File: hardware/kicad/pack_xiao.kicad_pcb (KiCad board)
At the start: 2 copper layers, 96 x 112 mm, 120 parts, among them U1 MCP1640T-I/CHY

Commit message: hardware: pack_xiao iron-only (plated holes under XIAO pads 16/20) and fits the enclosure (notch + cutout for the carrier posts)
Footprint XIAO_ESP32S3_SMD_THB (derived by tools/import_xiao.py) makes the two used bottom pads
plated holes, soldered from the board's back. gen_pcb learns NOTCH_BL and CUTOUTS (with a
no-copper fence, the router ignores edge clearance on inner circles); pack_xiao check_posts()
holds them to mech/params. make mech also gates --boards pack_xiao,carrier.

Co-Authored-By: Claude Opus 5.5 <noreply@anthropic.com>
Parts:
- removed the U_MCU at (78.0, 90.8)
- added U_MCU: XIAO ESP32-S3, local:XIAO_ESP32S3_SMD_THB, F.Cu at (76.0, 90.8)
- moved C_MCU1 2.00 mm to (55.5, 103.9)
- moved C_MCU2 2.00 mm to (55.5, 99.5)
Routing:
- net +3V3: track 170.5 -> 199.2 mm, vias 7 -> 6
- net VPACK: track 135.7 -> 111.4 mm, vias 2 -> 0
- net NTC3: track 84.0 -> 61.2 mm, vias 3 -> 2
- net SW1_DRV: track 120.3 -> 103.6 mm, vias 4 -> 2
- net CELL1_S: track 34.6 -> 18.2 mm, vias 0 -> 2
- net NTC2: track 102.6 -> 87.0 mm, vias 2 -> 0
- net CHG_CE: track 39.2 -> 54.4 mm
- net +5V: track 104.6 -> 91.6 mm
- net VMCU_IN: track 136.0 -> 147.3 mm
- net CC2: track 16.6 -> 26.9 mm, vias 0 -> 1
- net SYS_CHG: track 68.3 -> 58.0 mm, vias 4 -> 3
- net SW1_G: track 45.8 -> 55.7 mm
- net CELL4_G: track 22.1 -> 31.7 mm, vias 3 -> 2
- net SW3_DRV: track 66.9 -> 57.6 mm
- net SYS: track 107.8 -> 98.5 mm, vias 2 -> 0
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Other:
- outline, holes or cut-outs redrawn

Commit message: hardware: TME cost cuts (3 fewer resistor tapes, leaner spares); route.py survives KiCad 10's SWIG break
carrier_tme: R_OL/R_OR 470R -> 1k (DAC RC corner 72 kHz), R_LLB1/R_LLR1 0R -> 10R (button LEDs
have their own resistors). pack_xiao: R_GS1..4 1M -> 240k (17 uA per closed switch). Drops the
0805 0R, 470R and 1M tapes. tme_all: 1206 caps and the 0603 NTC get +10 % spares, no minimum 5.
About -44 PLN on the 5+5 order (order_35742850 prices).

route.py: stub_free moves from --finish to --import. Its connectivity rebuilds broke the SWIG type
table for the rest of the process, so finish() got bare SwigPyObjects for zones (carrier_tme
segfaulted in apport's excepthook on the AttributeError). Placement unchanged on both boards.

Co-Authored-By: Claude Opus 5.5 <noreply@anthropic.com>
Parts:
- R_GS1, R_GS2, R_GS3, R_GS4: value 1M -> 240k
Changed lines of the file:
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@@
 			)
 		)
-		(property "Value" "1M"
+		(property "Value" "240k"
 			(at 0 1.65 0)
 			(layer "F.Fab")
@@
 			)
 		)
-		(property "Value" "1M"
+		(property "Value" "240k"
 			(at 0 1.65 0)
 			(layer "F.Fab")
@@
 			)
 		)
-		(property "Value" "1M"
+		(property "Value" "240k"
 			(at 0 1.65 0)
 			(layer "F.Fab")
@@
 			)
 		)
-		(property "Value" "1M"
+		(property "Value" "240k"
 			(at 0 1.65 0)
 			(layer "F.Fab")

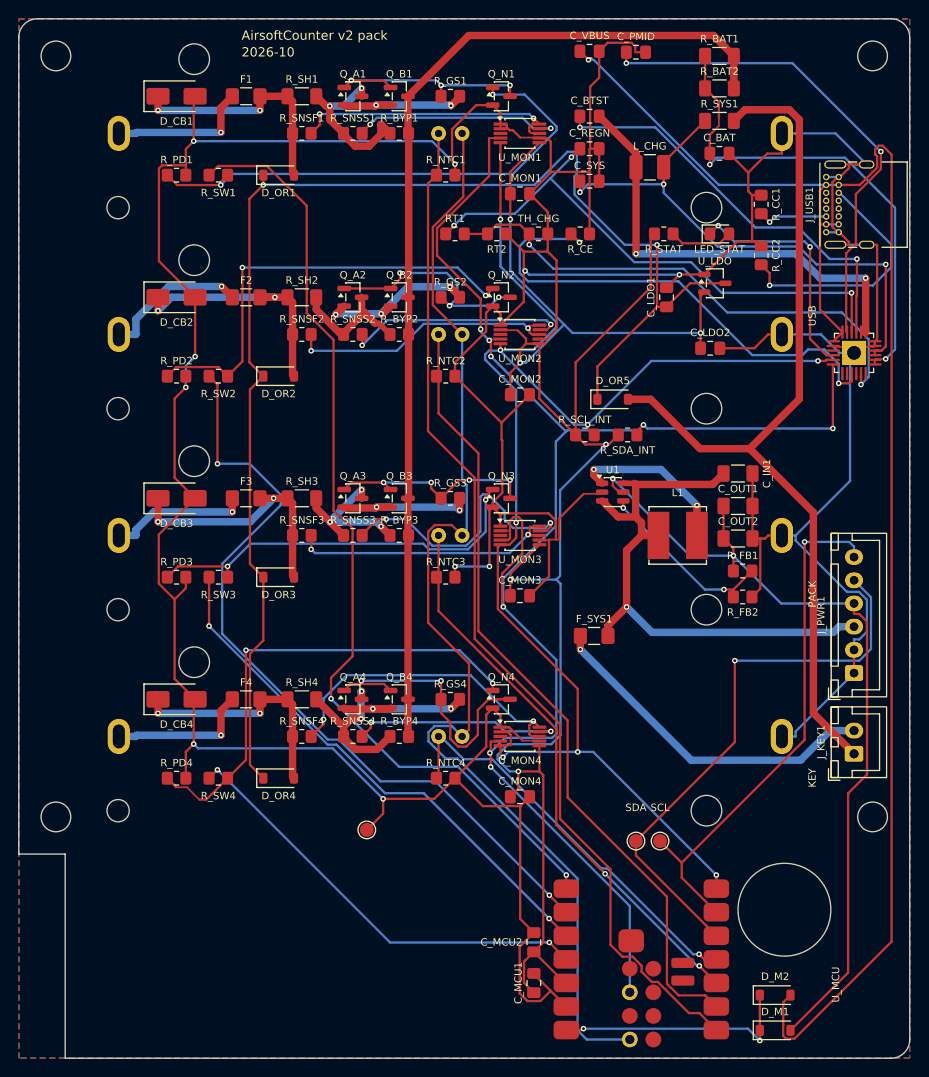
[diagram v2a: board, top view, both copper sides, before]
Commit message: hardware: cheaper TME equivalents; THB footprint in its own library; per-board KIID seed
TME swaps (user-picked, checked against each part's job): BSS138LT1G -> BSS138A-TP (all boards),
ERJ8BWFR010V -> Wayon MBR1206B5FR010S shunt, NTCS0603E3103FLT -> Murata NCU18XH103J6SRB (TH_CHG,
B3380 5 %: ~+-1.5 C on the charger limits), pack_xiao boost caps 22uF 25V -> CL31A226MOCLNNC 16 V
(5 V max; the LiPo keeps its 25 V parts).

Adding XIAO_ESP32S3_SMD_THB to local.pretty had renumbered every board using that library (KiCad
parses the whole library on first load, drawing on the seeded KIID sequence): pack_tme's footprint
order changed and Freerouting left a connection unrouted. The footprint moves to kicad/xiao.pretty;
pack_tme routes as before. gen_pcb takes KIID_SEED per board (default 1); pack_xiao uses 2.

Co-Authored-By: Claude Opus 5.5 <noreply@anthropic.com>
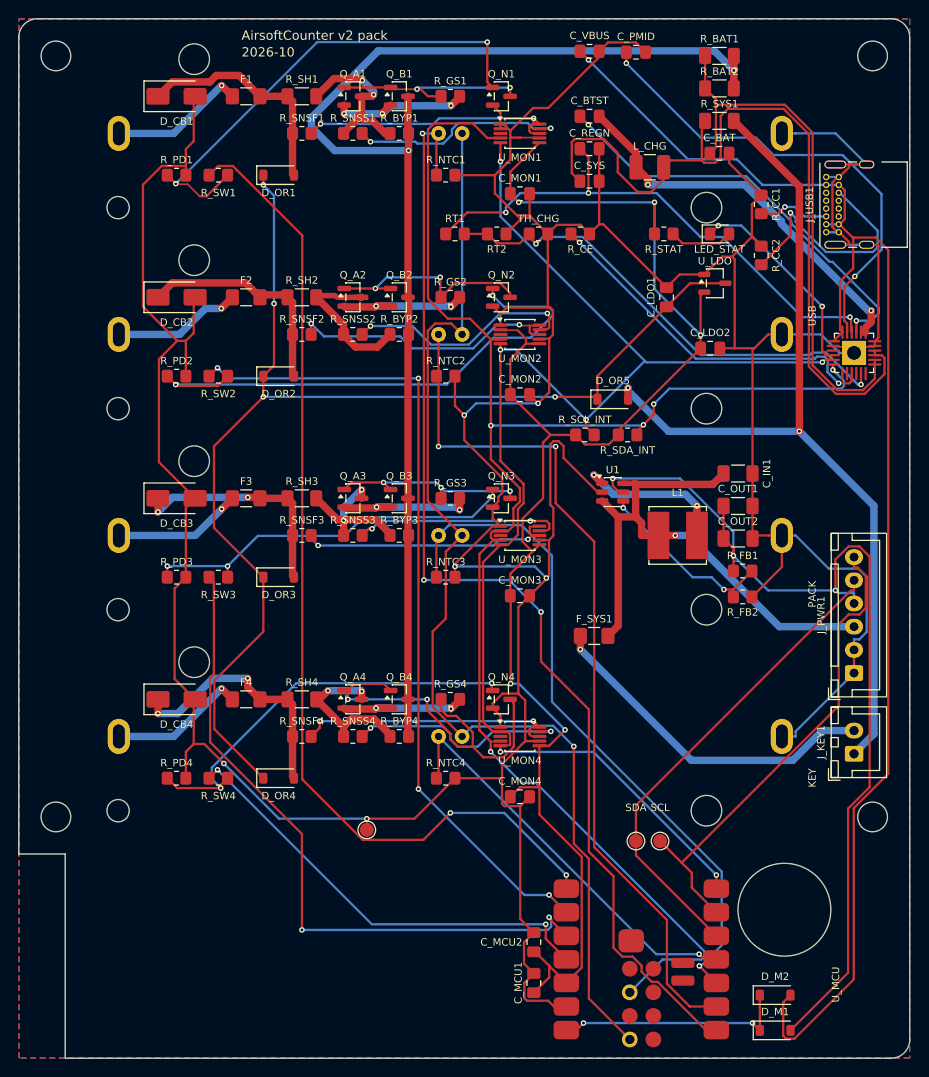
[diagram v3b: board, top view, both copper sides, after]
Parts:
- removed the U_MCU at (76.0, 90.8)
- added U_MCU: XIAO ESP32-S3, xiao:XIAO_ESP32S3_SMD_THB, F.Cu at (76.0, 90.8)
- C_IN1, C_OUT1, C_OUT2: value 22uF 25V -> 22uF 16V
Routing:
- net +3V3: track 199.2 -> 169.4 mm, vias 6 -> 5
- net SYS_CHG: track 58.0 -> 85.4 mm, vias 3 -> 0
- net VPACK: track 111.4 -> 134.6 mm, vias 0 -> 2
- net GND: track 559.6 -> 539.1 mm, vias 10 -> 6
- net VMCU_IN: track 147.3 -> 131.2 mm, vias 2 -> 4
- net SW3_DRV: track 57.6 -> 73.3 mm
- net CHG_CE: track 54.4 -> 38.8 mm
- net VBUS: track 169.4 -> 154.0 mm
- net +5V: track 91.6 -> 106.0 mm, vias 2 -> 3
- net NTC3: track 61.2 -> 74.1 mm, vias 2 -> 1
- net NTC1: track 111.6 -> 123.1 mm, vias 0 -> 3
- net SW2_G: track 48.2 -> 59.5 mm
- net CELL4_G: track 31.7 -> 40.9 mm
- net SDA_EXT: track 61.0 -> 51.8 mm, vias 1 -> 0
- net SNS_S3: track 30.8 -> 22.6 mm
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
